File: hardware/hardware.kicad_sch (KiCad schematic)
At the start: 15 parts, among them K1 RM85-2011-35-1005, K2 RM85-2011-35-1005, Q1 BC337, Q2 BC337, U1 XIAO-ESP32-C6, U2 DS18B20

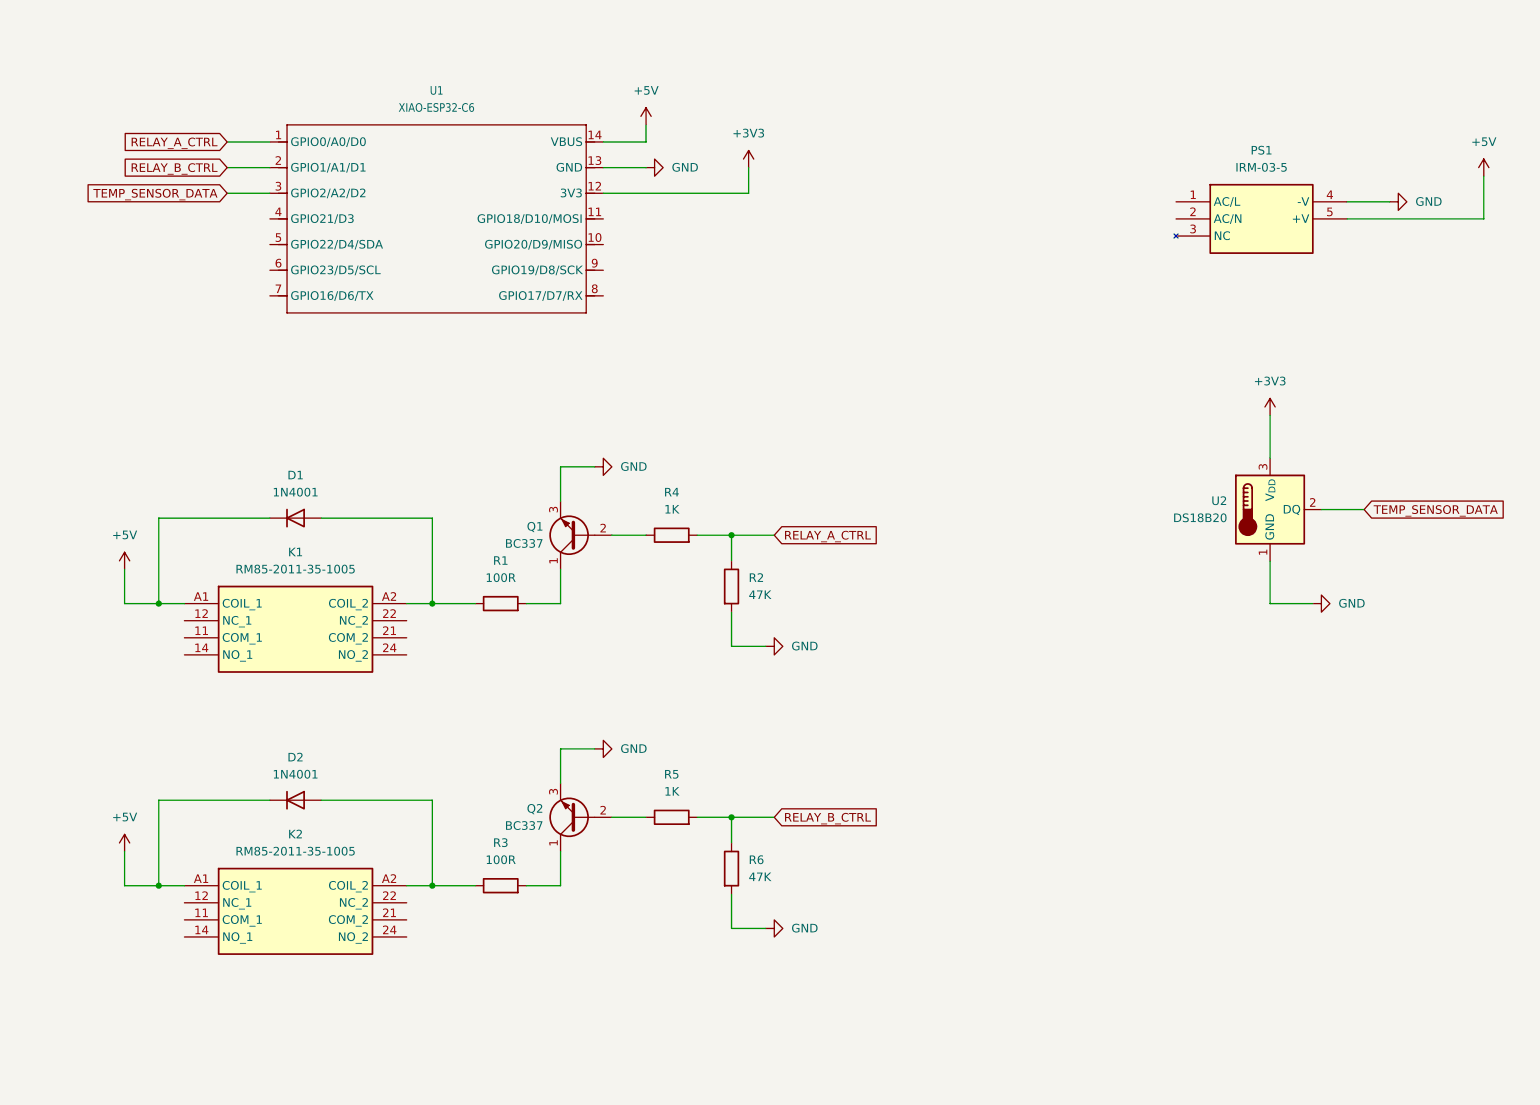
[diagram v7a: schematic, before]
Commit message: Added leds and connectors
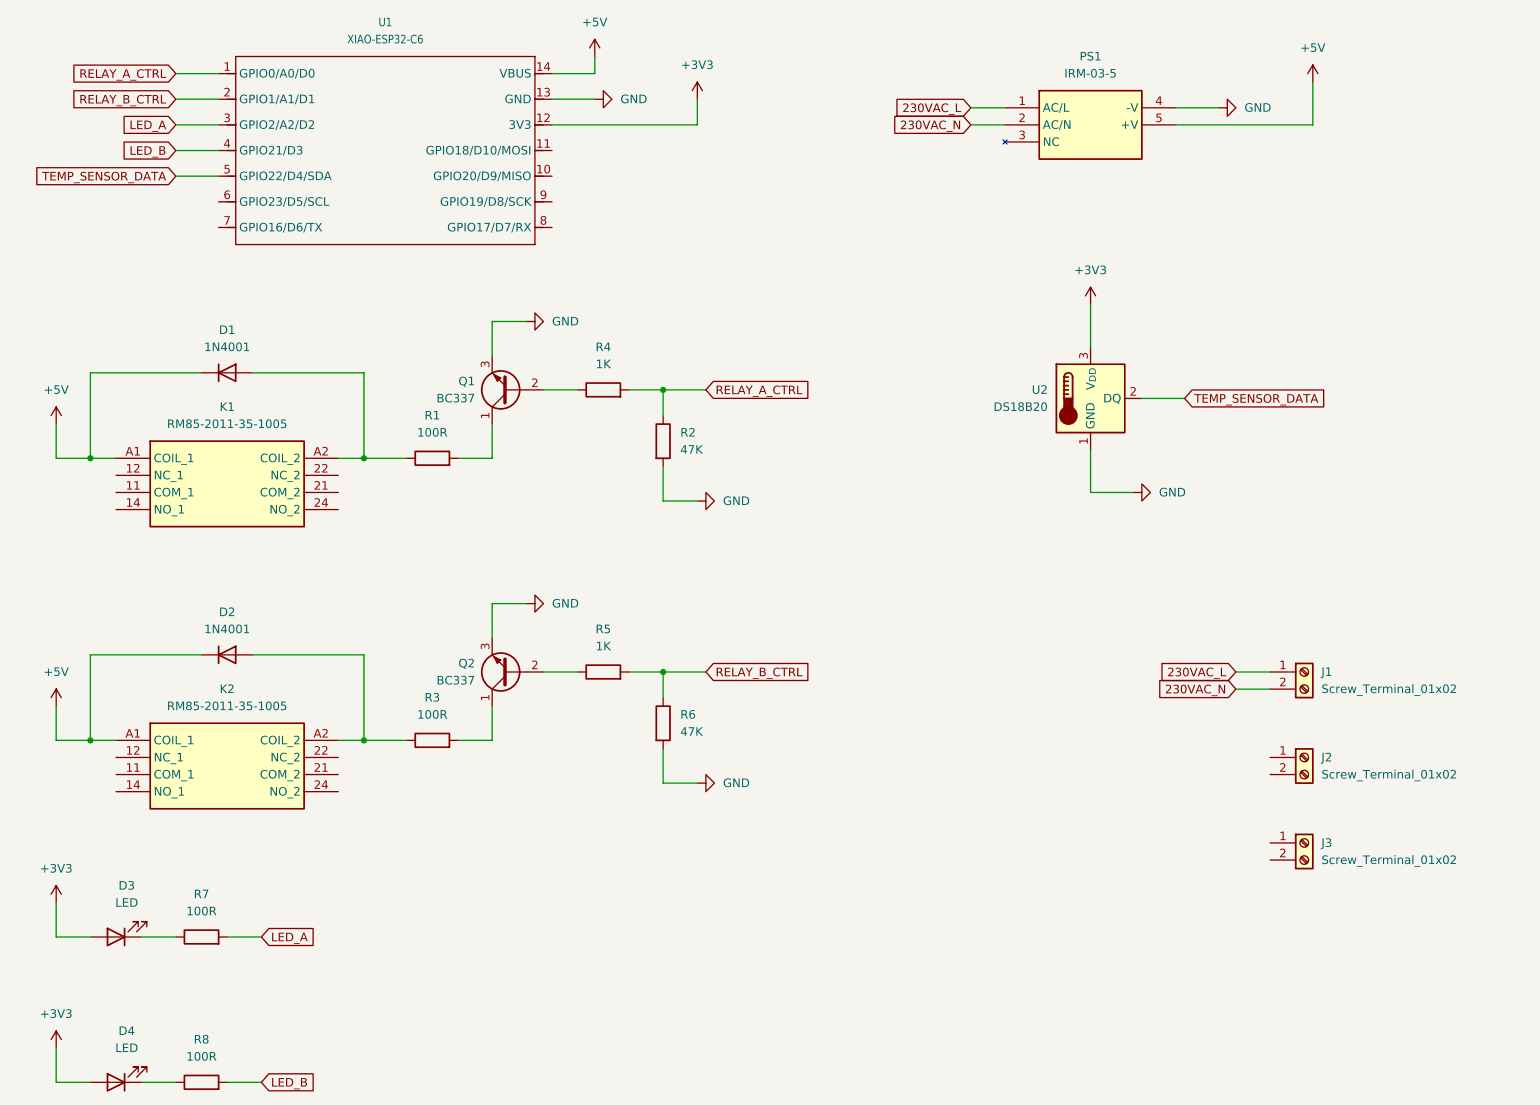
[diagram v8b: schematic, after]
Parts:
- added D3, D4: LED, LED_THT:LED_D5.0mm, symbol Device:LED
- added J1, J2, J3: Screw_Terminal_01x02, Degson Electronics:SHDR2W100P0X500_1X2_1000X780X1020P, symbol Connector:Screw_Terminal_01x02
- added R7, R8: 100R, Resistor_THT:R_Axial_DIN0204_L3.6mm_D1.6mm_P7.62mm_Horizontal, symbol Device:R
- R1, R2, R3, R4, R5, R6: footprint (none) -> Resistor_THT:R_Axial_DIN0204_L3.6mm_D1.6mm_P7.62mm_Horizontal
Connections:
- net +3V3: now also D3.2 (A), D4.2 (A)
- net TEMP_SENSOR_DATA: now also U1.5 (GPIO22/D4/SDA); no longer U1.3 (GPIO2/A2/D2)
- net 230VAC_L: now reaches PS1.1 (AC/L)
- net 230VAC_L: now also J1.1 (Pin_1)
- net 230VAC_N: now reaches PS1.2 (AC/N)
- net 230VAC_N: now also J1.2 (Pin_2)
- net LED_B: now reaches U1.4 (GPIO21/D3)
- net LED_B: now also R8.2
- new net: D4.1 (K), R8.1
- new net: D3.1 (K), R7.1
- new net LED_A: R7.2, U1.3 (GPIO2/A2/D2)
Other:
- moved on the sheet: D1, D2, K1, K2, PS1, Q1, Q2, R1, R2, R3, R4, R5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
